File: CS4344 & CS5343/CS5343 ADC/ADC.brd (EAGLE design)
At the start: 29 x 17 mm, 21 parts

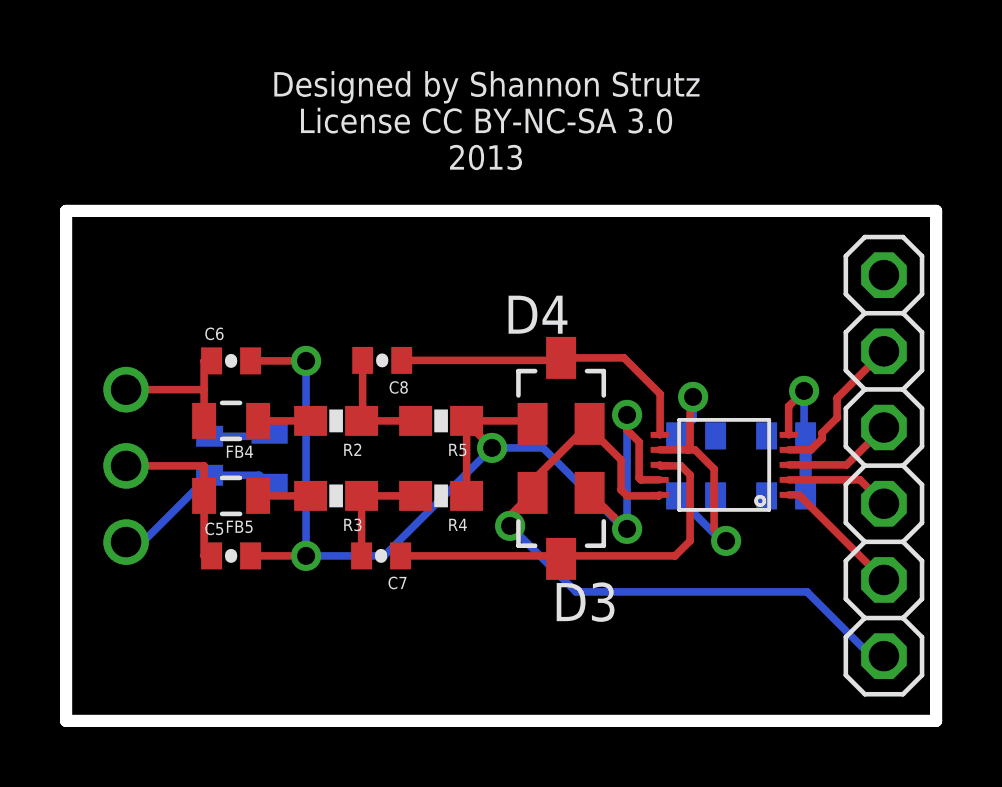
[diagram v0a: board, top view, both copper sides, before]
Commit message: Update DAC,ADC, and ADSP
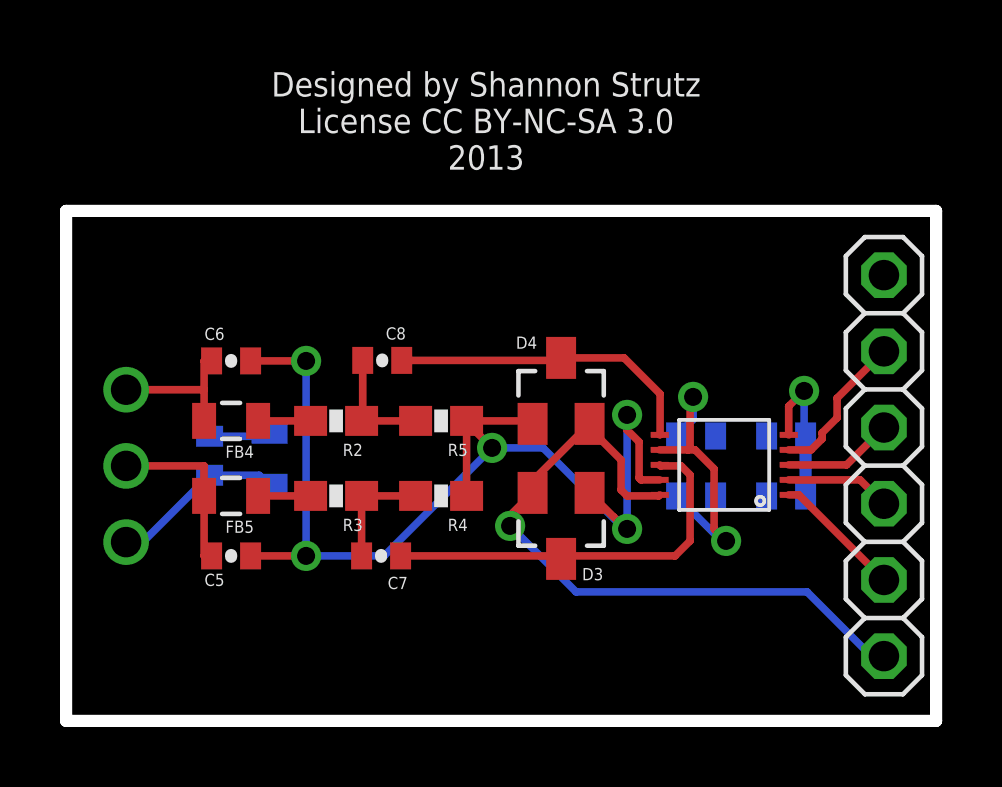
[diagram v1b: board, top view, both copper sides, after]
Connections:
- net N$5 renamed MCLK
- net N$7 renamed LRCLK
- net N$8 renamed SCLK
- net N$9 renamed SOUT
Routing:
- added copper zone on layer 1, net GND
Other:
- board text added: "CS5343 24-bit I2S ADC Eval Shannon Strutz"
- board text added: "GND"
- board text added: "LEFT"
- board text added: "LR"
- board text added: "MCLK"
- board text added: "RIGHT"
- board text added: "SCLK"
- board text added: "SLEEVE"
- board text added: "SOUT"
- board text added: "VCC"
- board text removed: "CS5343 24-bit I2S ADC EVM Shannon Strutz"
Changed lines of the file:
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@@
 <?xml version="1.0" encoding="utf-8"?>
 <!DOCTYPE eagle SYSTEM "eagle.dtd">
-<eagle version="6.4">
+<eagle version="6.5.0">
 <drawing>
 <settings>
@@
 <wire x1="0" y1="17" x2="0" y2="0" width="0.4064" layer="20"/>
 <wire x1="0" y1="0" x2="29" y2="0" width="0.4064" layer="20"/>
-<text x="11.1" y="8.1" size="0.8128" layer="122" rot="R180" align="center">CS5343 24-bit
+<text x="10.9" y="8.5" size="0.8128" layer="122" rot="MR180" align="center">CS5343 24-bit
 I2S ADC
-EVM
+Eval
 Shannon
 Strutz</text>
@@
 License CC BY-NC-SA 3.0
 2013</text>
+<text x="1.7" y="12.5" size="0.4064" layer="122" rot="MR90">LEFT</text>
+<text x="3.5" y="7.7" size="0.4064" layer="122" rot="MR90">RIGHT</text>
+<text x="1.9" y="2.3" size="0.4064" layer="122" rot="MR90">SLEEVE</text>
+<text x="25.7" y="14.7" size="0.4064" layer="122" rot="MR0">GND</text>
+<text x="25.8" y="12.1" size="0.4064" layer="122" rot="MR0">MCLK</text>
+<text x="25.8" y="9.5" size="0.4064" layer="122" rot="MR0">LR</text>
+<text x="25.8" y="4.5" size="0.4064" layer="122" rot="MR0">SOUT</text>
+<text x="25.8" y="6" size="0.4064" layer="122" rot="MR0">SCLK</text>
+<wire x1="25.3" y1="6.6" x2="25.3" y2="7.1" width="0.1" layer="122"/>
+<wire x1="25.3" y1="7.1" x2="25.5" y2="7.3" width="0.1" layer="122"/>
+<wire x1="25.5" y1="7.3" x2="25.8" y2="7.3" width="0.1" layer="122"/>
+<wire x1="25.8" y1="7.3" x2="25.6" y2="7.5" width="0.1" layer="122"/>
+<wire x1="25.6" y1="7.5" x2="25.6" y2="7.1" width="0.1" layer="122"/>
+<wire x1="25.6" y1="7.1" x2="25.8" y2="7.3" width="0.1" layer="122"/>
+<text x="25.8" y="2" size="0.4064" layer="122" rot="MR0">VCC</text>
 </plain>
 <attributes>
@@
 </autorouter>
 <elements>
-<element name="FB4" library="SparkFun-Passives" package="0805" value="220" x="5.5" y="10" rot="R180"/>
-<element name="FB5" library="SparkFun-Passives" package="0805" value="220" x="5.5" y="7.5" rot="R180"/>
-<element name="FB6" library="SparkFun-Passives" package="0805" value="220" x="6.7836" y="8.7366" rot="MR270"/>
-<element name="C4" library="1x05smd" package="0402-CAP" value="1000pF" x="4.7836" y="8.8366" rot="MR90"/>
-<element name="C5" library="1x05smd" package="0402-CAP" value="1000pF" x="5.5" y="5.5"/>
-<element name="C6" library="1x05smd" package="0402-CAP" value="1000pF" x="5.5" y="12"/>
-<element name="U$3" library="Strutz Electronic Industries" package="TSSOP-10" value="CS5343" x="21.9366" y="8.5336" rot="R180"/>
-<element name="R2" library="1x05smd" package="0603-RES" value="6.81k" x="9" y="10" rot="R180"/>
-<element name="R3" library="1x05smd" package="0603-RES" value="6.81k" x="9" y="7.5" rot="R180"/>
-<element name="R4" library="1x05smd" package="0603-RES" value="3.32k" x="12.5" y="7.5" rot="R180"/>
-<element name="R5" library="1x05smd" package="0603-RES" value="3.32k" x="12.5" y="10" rot="R180"/>
-<element name="C7" library="1x05smd" package="0402-CAP" value="1uF" x="10.5" y="5.5" rot="R180"/>
-<element name="C8" library="1x05smd" package="0402-CAP" value="1uF" x="10.5366" y="12.0164" rot="R180"/>
-<element name="D3" library="diode" package="SOT23" value="BAT54S" x="16.5" y="6.5" rot="R180"/>
-<element name="D4" library="diode" package="SOT23" value="BAT54S" x="16.5" y="11"/>
-<element name="C13" library="1x05smd" package="0402-CAP" value=".1uF" x="21" y="9.5" rot="MR0"/>
-<element name="C14" library="1x05smd" package="0402-CAP" value=".1uF" x="24" y="7.5" rot="MR0"/>
-<element name="C15" library="1x05smd" package="0402-CAP" value="1uF" x="21" y="7.5" rot="MR0"/>
-<element name="C19" library="1x05smd" package="0402-CAP" value="1uF" x="24" y="9.5" rot="MR0"/>
+<element name="FB4" library="SparkFun-Passives" package="0805" value="220" x="5.5" y="10" smashed="yes" rot="R180">
+<attribute name="NAME" x="6.262" y="9.1745" size="0.4064" layer="25" rot="R180"/>
+</element>
+<element name="FB5" library="SparkFun-Passives" package="0805" value="220" x="5.5" y="7.5" smashed="yes" rot="R180">
+<attribute name="NAME" x="6.262" y="6.6745" size="0.4064" layer="25" rot="R180"/>
+</element>
+<element name="FB6" library="SparkFun-Passives" package="0805" value="220" x="6.7836" y="8.7366" smashed="yes" rot="MR270">
+<attribute name="NAME" x="5.9581" y="9.4986" size="0.4064" layer="26" rot="MR270"/>
+</element>
+<element name="C4" library="1x05smd" package="0402-CAP" value="1000pF" x="4.7836" y="8.8366" smashed="yes" rot="MR90">
+<attribute name="NAME" x="5.4821" y="7.9476" size="0.4064" layer="26" rot="MR90"/>
+</element>
+<element name="C5" library="1x05smd" package="0402-CAP" value="1000pF" x="5.5" y="5.5" smashed="yes">
+<attribute name="NAME" x="4.611" y="4.4985" size="0.4064" layer="25"/>
+</element>
+<element name="C6" library="1x05smd" package="0402-CAP" value="1000pF" x="5.5" y="12" smashed="yes">
+<attribute name="NAME" x="4.611" y="12.6985" size="0.4064" layer="25"/>
+</element>
+<element name="U$3" library="Strutz Electronic Industries" package="TSSOP-10" value="CS5343" x="21.9366" y="8.5336" smashed="yes" rot="R180"/>
+<element name="R2" library="1x05smd" package="0603-RES" value="6.81k" x="9" y="10" smashed="yes" rot="R180">
+<attribute name="NAME" x="9.889" y="9.238" size="0.4064" layer="25" font="vector" rot="R180"/>
+</element>
+<element name="R3" library="1x05smd" package="0603-RES" value="6.81k" x="9" y="7.5" smashed="yes" rot="R180">
+<attribute name="NAME" x="9.889" y="6.738" size="0.4064" layer="25" font="vector" rot="R180"/>
+</element>
+<element name="R4" library="1x05smd" package="0603-RES" value="3.32k" x="12.5" y="7.5" smashed="yes" rot="R180">
+<attribute name="NAME" x="13.389" y="6.738" size="0.4064" layer="25" font="vector" rot="R180"/>
+</element>
+<element name="R5" library="1x05smd" package="0603-RES" value="3.32k" x="12.5" y="10" smashed="yes" rot="R180">
+<attribute name="NAME" x="13.389" y="9.238" size="0.4064" layer="25" font="vector" rot="R180"/>
+</element>
+<element name="C7" library="1x05smd" package="0402-CAP" value="1uF" x="10.5" y="5.5" smashed="yes" rot="R180">
+<attribute name="NAME" x="11.389" y="4.8015" size="0.4064" layer="25" rot="R180"/>
+</element>
+<element name="C8" library="1x05smd" package="0402-CAP" value="1uF" x="10.5366" y="12.0164" smashed="yes" rot="R180">
+<attribute name="NAME" x="11.3256" y="13.1179" size="0.4064" layer="25" rot="R180"/>
+</element>
+<element name="D3" library="diode" package="SOT23" value="BAT54S" x="16.5" y="6.5" smashed="yes" rot="R180">
+<attribute name="NAME" x="17.905" y="5.095" size="0.4064" layer="25" rot="R180"/>
+</element>
+<element name="D4" library="diode" package="SOT23" value="BAT54S" x="16.5" y="11" smashed="yes">
+<attribute name="NAME" x="14.995" y="12.405" size="0.4064" layer="25"/>
+</element>
+<element name="C13" library="1x05smd" package="0402-CAP" value=".1uF" x="21" y="9.5" smashed="yes" rot="MR0">
+<attribute name="NAME" x="21.889" y="10.1985" size="0.4064" layer="26" rot="MR0"/>
+</element>
+<element name="C14" library="1x05smd" package="0402-CAP" value=".1uF" x="24" y="7.5" smashed="yes" rot="MR0">
+<attribute name="NAME" x="24.889" y="8.1985" size="0.4064" layer="26" rot="MR0"/>
+</element>
+<element name="C15" library="1x05smd" package="0402-CAP" value="1uF" x="21" y="7.5" smashed="yes" rot="MR0">
+<attribute name="NAME" x="21.889" y="8.1985" size="0.4064" layer="26" rot="MR0"/>
+</element>
+<element name="C19" library="1x05smd" package="0402-CAP" value="1uF" x="24" y="9.5" smashed="yes" rot="MR0">
+<attribute name="NAME" x="24.889" y="10.1985" size="0.4064" layer="26" rot="MR0"/>
+</element>
 <element name="JP1" library="adafruit" package="1X06" value="" x="27.2616" y="8.5086" smashed="yes" rot="R270">
 <attribute name="VALUE" x="24.0866" y="16.1286" size="1.27" layer="27" rot="R270"/>
@@
 <via x="8" y="12" extent="1-16" drill="0.6"/>
 <wire x1="8" y1="12" x2="8" y2="5.5" width="0.254" layer="16"/>
+<polygon width="0.4064" layer="1">
+<vertex x="0" y="17"/>
+<vertex x="29" y="17"/>
+<vertex x="29" y="0"/>
+<vertex x="0" y="0"/>
+</polygon>
 </signal>
 <signal name="VCC">
@@
 <wire x1="24.6" y1="9.55" x2="24.65" y2="9.5" width="0.254" layer="16"/>
 </signal>
-<signal name="N$5">
+<signal name="MCLK">
 <contactref element="JP1" pad="2"/>
 <contactref element="U$3" pad="4"/>
@@
 <wire x1="25.7" y1="10.757" x2="27.2616" y2="12.3186" width="0.254" layer="1"/>
 </signal>
-<signal name="N$7">
+<signal name="LRCLK">
 <contactref element="JP1" pad="3"/>
 <contactref element="U$3" pad="3"/>
@@
 <wire x1="26.0166" y1="8.5336" x2="27.2616" y2="9.7786" width="0.254" layer="1"/>
 </signal>
-<signal name="N$8">
+<signal name="SCLK">
 <contactref element="JP1" pad="4"/>
 <contactref element="U$3" pad="2"/>
@@
 <wire x1="26.4666" y1="8.0336" x2="27.2616" y2="7.2386" width="0.254" layer="1"/>
 </signal>
-<signal name="N$9">
+<signal name="SOUT">
 <contactref element="JP1" pad="5"/>
 <contactref element="U$3" pad="1"/>
